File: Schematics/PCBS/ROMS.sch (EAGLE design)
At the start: 10 parts, among them IC1 ATMEGA328P-AU, M1 WIRELESS-NRF24L01-PA-EXT, Y1 16MHz

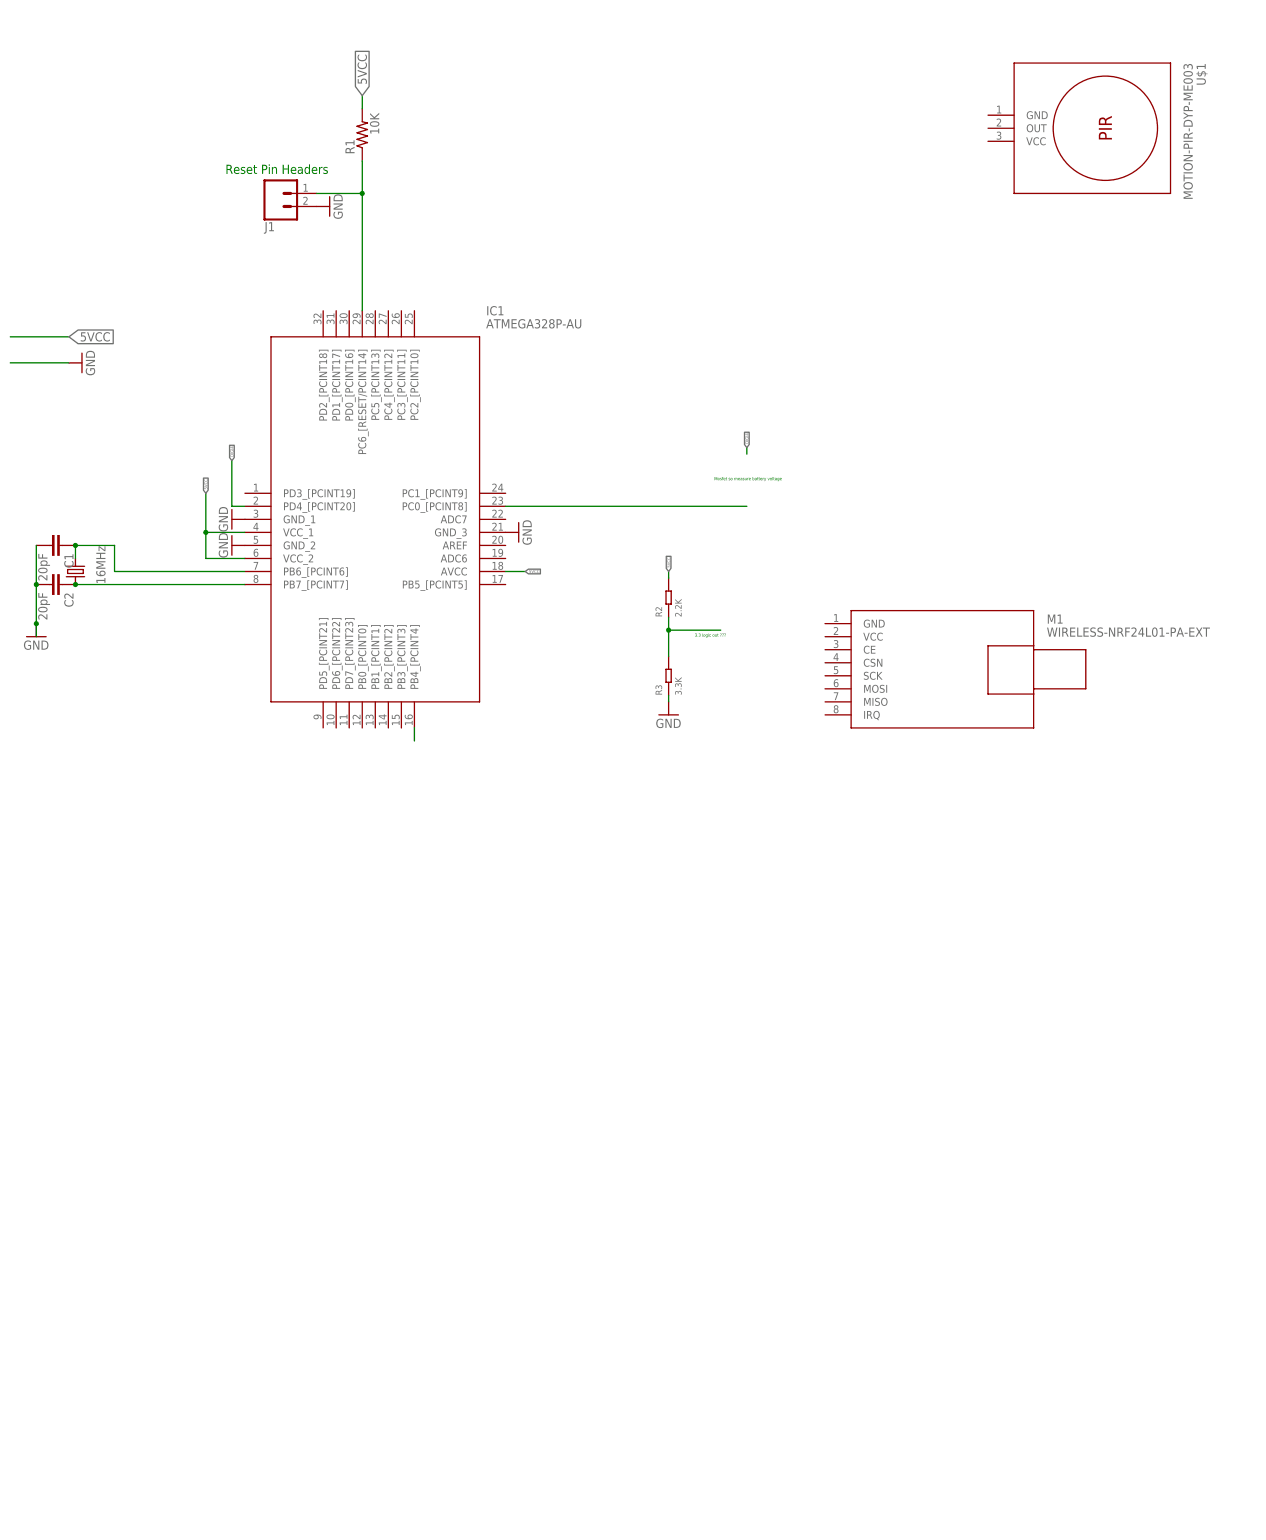
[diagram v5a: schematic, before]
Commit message: added header pins for IR Sensor
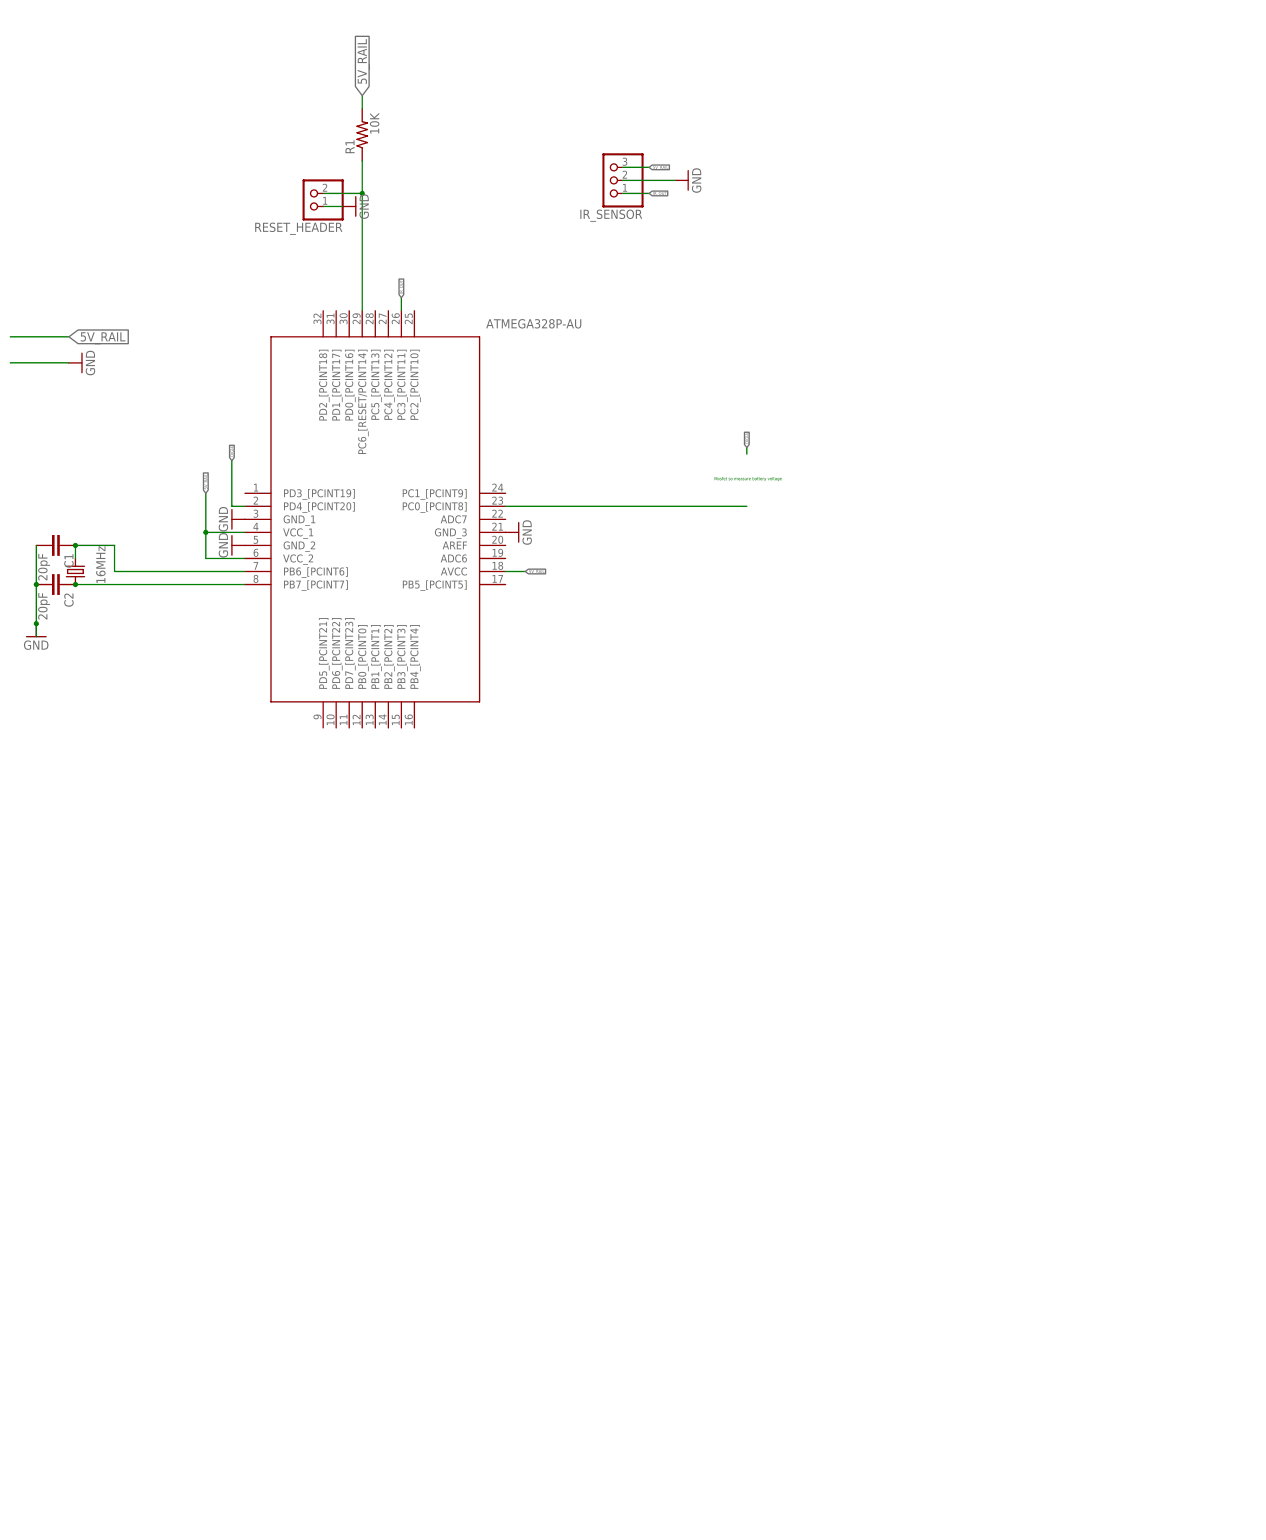
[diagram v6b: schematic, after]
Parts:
- removed J1: (no value), SparkFun-Connectors:CONN_02
- removed M1: WIRELESS-NRF24L01-PA-EXT, diy-modules:WIRELESS-NRF24L01-PA-EXT
- removed R2: 2.2K, Seeed-Resistor-2016:DIP-RES-2.2K-5%-1/4W(PR-D2.3XL6.5MM)
- removed R3: 3.3K, Seeed-Resistor-2016:DIP-RES-3.3K-5%-1/4W(PR-D2.3XL6.5MM)
- removed U$1: MOTION-PIR-DYP-ME003, diy-modules:MOTION-PIR-DYP-ME003
- added IR_SENSOR: (no value), adafruit:PINHD-1X3
- added RESET_HEADER: (no value), Connector:PINHD-1X2
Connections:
- removed net 5VCC: IC1.AVCC, IC1.VCC_1, IC1.VCC_2, R1.2, R2.2
- removed net N$5: R2.1, R3.2
- removed net N$6: IC1.PB4_[PCINT4]
- new net 5V_RAIL: IC1.AVCC, IC1.VCC_1, IC1.VCC_2, IR_SENSOR.3, R1.2
- new net IR_OUT: IC1.PC3_[PCINT11], IR_SENSOR.1
- net GND: now also IR_SENSOR.2, RESET_HEADER.1; no longer J1.2, R3.1
- net N$3: now also RESET_HEADER.2; no longer J1.1
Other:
- note removed: "3.3 logic out ???"
- note removed: "Reset Pin Headers"
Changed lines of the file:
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@@
 <?xml version="1.0" encoding="utf-8"?>
 <!DOCTYPE eagle SYSTEM "eagle.dtd">
-<eagle version="9.5.2">
+<eagle version="9.6.2">
 <drawing>
 <settings>
@@
 <part name="GND5" library="supply1" library_urn="urn:adsk.eagle:library:371" deviceset="GND" device=""/>
 <part name="R1" library="adafruit" library_urn="urn:adsk.eagle:library:420" deviceset="R-US_" device="0207/10" package3d_urn="urn:adsk.eagle:package:6240597/1" value="10K"/>
-<part name="J1" library="SparkFun-Connectors" deviceset="CONN_02" device=""/>
 <part name="GND6" library="supply1" library_urn="urn:adsk.eagle:library:371" deviceset="GND" device=""/>
-<part name="U$1" library="diy-modules" deviceset="MOTION-PIR-DYP-ME003" device=""/>
-<part name="M1" library="diy-modules" deviceset="WIRELESS-NRF24L01-PA-EXT" device=""/>
-<part name="R2" library="Seeed-Resistor-2016" deviceset="DIP-RES-2.2K-5%-1/4W(PR-D2.3XL6.5MM)" device="" value="2.2K"/>
-<part name="R3" library="Seeed-Resistor-2016" deviceset="DIP-RES-3.3K-5%-1/4W(PR-D2.3XL6.5MM)" device="" value="3.3K"/>
+<part name="IR_SENSOR" library="adafruit" library_urn="urn:adsk.eagle:library:420" deviceset="PINHD-1X3" device="" package3d_urn="urn:adsk.eagle:package:6240710/1"/>
 <part name="GND7" library="supply1" library_urn="urn:adsk.eagle:library:371" deviceset="GND" device=""/>
+<part name="RESET_HEADER" library="Connector" library_urn="urn:adsk.eagle:library:16378166" deviceset="PINHD-1X2" device="" package3d_urn="urn:adsk.eagle:package:22435/2"/>
 </parts>
 <sheets>
 <sheet>
 <plain>
-<text x="46.99" y="110.49" size="1.778" layer="91">Reset Pin Headers</text>
 <text x="142.24" y="50.8" size="0.6096" layer="91">Mosfet so measure battery voltage</text>
-<text x="138.43" y="20.32" size="0.6096" layer="91">3.3 logic out ???</text>
 </plain>
 <instances>
 <instance part="IC1" gate="G$1" x="50.8" y="48.26" smashed="yes">
-<attribute name="NAME" x="97.79" y="83.82" size="1.778" layer="95" align="center-left"/>
 <attribute name="VALUE" x="97.79" y="81.28" size="1.778" layer="96" align="center-left"/>
 </instance>
@@
 <attribute name="VALUE" x="76.962" y="118.11" size="1.778" layer="96" rot="R90"/>
 </instance>
-<instance part="J1" gate="G$1" x="57.15" y="106.68" smashed="yes" rot="MR180">
-<attribute name="VALUE" x="54.61" y="111.506" size="1.778" layer="96" font="vector" rot="MR180"/>
-<attribute name="NAME" x="54.61" y="101.092" size="1.778" layer="95" font="vector" rot="MR180"/>
-</instance>
-<instance part="GND6" gate="1" x="67.31" y="104.14" smashed="yes" rot="R90">
-<attribute name="VALUE" x="69.85" y="101.6" size="1.778" layer="96" rot="R90"/>
-</instance>
-<instance part="U$1" gate="G$1" x="215.9" y="119.38" smashed="yes" rot="R270">
-<attribute name="NAME" x="236.22" y="132.08" size="1.778" layer="95" rot="R270"/>
-<attribute name="VALUE" x="233.68" y="132.08" size="1.778" layer="96" rot="R270"/>
-</instance>
-<instance part="M1" gate="G$1" x="186.69" y="12.7" smashed="yes">
-<attribute name="NAME" x="207.01" y="22.86" size="1.778" layer="95"/>
-<attribute name="VALUE" x="207.01" y="20.32" size="1.778" layer="96"/>
-</instance>
-<instance part="R2" gate="G$1" x="133.35" y="27.94" smashed="yes" rot="R90">
-<attribute name="NAME" x="132.08" y="24.13" size="1.27" layer="95" ratio="10" rot="R90"/>
-<attribute name="VALUE" x="135.89" y="24.13" size="1.27" layer="96" ratio="10" rot="R90"/>
-</instance>
-<instance part="R3" gate="G$1" x="133.35" y="12.7" smashed="yes" rot="R90">
-<attribute name="NAME" x="132.08" y="8.89" size="1.27" layer="95" ratio="10" rot="R90"/>
-<attribute name="VALUE" x="135.89" y="8.89" size="1.27" layer="96" ratio="10" rot="R90"/>
-</instance>
-<instance part="GND7" gate="1" x="133.35" y="5.08" smashed="yes">
-<attribute name="VALUE" x="130.81" y="2.54" size="1.778" layer="96"/>
+<instance part="GND6" gate="1" x="72.39" y="104.14" smashed="yes" rot="R90">
+<attribute name="VALUE" x="74.93" y="101.6" size="1.778" layer="96" rot="R90"/>
+</instance>
+<instance part="IR_SENSOR" gate="A" x="121.92" y="109.22" smashed="yes" rot="R180">
+<attribute name="NAME" x="128.27" y="103.505" size="1.778" layer="95" rot="R180"/>
+<attribute name="VALUE" x="128.27" y="116.84" size="1.778" layer="96" rot="R180"/>
+</instance>
+<instance part="GND7" gate="1" x="137.16" y="109.22" smashed="yes" rot="R90">
+<attribute name="VALUE" x="139.7" y="106.68" size="1.778" layer="96" rot="R90"/>
+</instance>
+<instance part="RESET_HEADER" gate="G$1" x="63.5" y="106.68" smashed="yes" rot="R180">
+<attribute name="NAME" x="69.85" y="100.965" size="1.778" layer="95" rot="R180"/>
+<attribute name="VALUE" x="69.85" y="111.76" size="1.778" layer="96" rot="R180"/>
 </instance>
 </instances>
@@
 </segment>
 <segment>
-<pinref part="J1" gate="G$1" pin="2"/>
+<pinref part="IR_SENSOR" gate="A" pin="2"/>
+<wire x1="124.46" y1="109.22" x2="134.62" y2="109.22" width="0.1524" layer="91"/>
+<pinref part="GND7" gate="1" pin="GND"/>
+</segment>
+<segment>
 <pinref part="GND6" gate="1" pin="GND"/>
-</segment>
-<segment>
-<pinref part="R3" gate="G$1" pin="1"/>
-<pinref part="GND7" gate="1" pin="GND"/>
-<wire x1="133.35" y1="8.89" x2="133.35" y2="7.62" width="0.1524" layer="91"/>
-</segment>
-</net>
-<net name="5VCC" class="0">
+<pinref part="RESET_HEADER" gate="G$1" pin="1"/>
+<wire x1="69.85" y1="104.14" x2="66.04" y2="104.14" width="0.1524" layer="91"/>
+</segment>
+</net>
+<net name="N$3" class="0">
+<segment>
+<pinref part="IC1" gate="G$1" pin="PC6_[RESET/PCINT14]"/>
+<pinref part="R1" gate="G$1" pin="1"/>
+<wire x1="73.66" y1="83.82" x2="73.66" y2="106.68" width="0.1524" layer="91"/>
+<pinref part="RESET_HEADER" gate="G$1" pin="2"/>
+<wire x1="73.66" y1="106.68" x2="73.66" y2="113.03" width="0.1524" layer="91"/>
+<wire x1="73.66" y1="106.68" x2="66.04" y2="106.68" width="0.1524" layer="91"/>
+<junction x="73.66" y="106.68"/>
+</segment>
+</net>
+<net name="N$4" class="0">
+<segment>
+<pinref part="IC1" gate="G$1" pin="PC0_[PCINT8]"/>
+<wire x1="101.6" y1="45.72" x2="148.59" y2="45.72" width="0.1524" layer="91"/>
+</segment>
+</net>
+<net name="DIGI4" class="0">
+<segment>
+<pinref part="IC1" gate="G$1" pin="PD4_[PCINT20]"/>
+<wire x1="50.8" y1="45.72" x2="48.26" y2="45.72" width="0.1524" layer="91"/>
+<wire x1="48.26" y1="45.72" x2="48.26" y2="54.61" width="0.1524" layer="91"/>
+<label x="48.26" y="54.61" size="0.6096" layer="95" rot="R90" xref="yes"/>
+</segment>
+<segment>
+<wire x1="148.59" y1="55.88" x2="148.59" y2="57.15" width="0.1524" layer="91"/>
+<label x="148.59" y="57.15" size="0.6096" layer="95" rot="R90" xref="yes"/>
+</segment>
+</net>
+<net name="5V_RAIL" class="0">
 <segment>
 <wire x1="5.08" y1="78.74" x2="16.51" y2="78.74" width="0.1524" layer="91"/>
@@
 </segment>
 <segment>
-<pinref part="R2" gate="G$1" pin="2"/>
-<wire x1="133.35" y1="31.75" x2="133.35" y2="33.02" width="0.1524" layer="91"/>
-<label x="133.35" y="33.02" size="0.6096" layer="95" rot="R90" xref="yes"/>
-</segment>
-</net>
-<net name="N$3" class="0">
-<segment>
-<pinref part="IC1" gate="G$1" pin="PC6_[RESET/PCINT14]"/>
-<pinref part="R1" gate="G$1" pin="1"/>
-<wire x1="73.66" y1="83.82" x2="73.66" y2="106.68" width="0.1524" layer="91"/>
-<pinref part="J1" gate="G$1" pin="1"/>
-<wire x1="73.66" y1="106.68" x2="73.66" y2="113.03" width="0.1524" layer="91"/>
-<wire x1="64.77" y1="106.68" x2="73.66" y2="106.68" width="0.1524" layer="91"/>
-<junction x="73.66" y="106.68"/>
-</segment>
-</net>
-<net name="N$4" class="0">
-<segment>
-<pinref part="IC1" gate="G$1" pin="PC0_[PCINT8]"/>
-<wire x1="101.6" y1="45.72" x2="148.59" y2="45.72" width="0.1524" layer="91"/>
-</segment>
-</net>
-<net name="DIGI4" class="0">
-<segment>
-<pinref part="IC1" gate="G$1" pin="PD4_[PCINT20]"/>
-<wire x1="50.8" y1="45.72" x2="48.26" y2="45.72" width="0.1524" layer="91"/>
-<wire x1="48.26" y1="45.72" x2="48.26" y2="54.61" width="0.1524" layer="91"/>
-<label x="48.26" y="54.61" size="0.6096" layer="95" rot="R90" xref="yes"/>
-</segment>
-<segment>
-<wire x1="148.59" y1="55.88" x2="148.59" y2="57.15" width="0.1524" layer="91"/>
-<label x="148.59" y="57.15" size="0.6096" layer="95" rot="R90" xref="yes"/>
-</segment>
-</net>
-<net name="N$5" class="0">
-<segment>
-<pinref part="R3" gate="G$1" pin="2"/>
-<pinref part="R2" gate="G$1" pin="1"/>
-<wire x1="133.35" y1="16.51" x2="133.35" y2="21.59" width="0.1524" layer="91"/>
-<wire x1="133.35" y1="21.59" x2="133.35" y2="24.13" width="0.1524" layer="91"/>
-<wire x1="133.35" y1="21.59" x2="143.51" y2="21.59" width="0.1524" layer="91"/>
-<junction x="133.35" y="21.59"/>
-</segment>
-</net>
-<net name="N$6" class="0">
-<segment>
-<pinref part="IC1" gate="G$1" pin="PB4_[PCINT4]"/>
-<wire x1="83.82" y1="2.54" x2="83.82" y2="0" width="0.1524" layer="91"/>
-</segment>
-</net>
+<pinref part="IR_SENSOR" gate="A" pin="3"/>
+<wire x1="124.46" y1="111.76" x2="129.54" y2="111.76" width="0.1524" layer="91"/>
+<label x="129.54" y="111.76" size="0.6096" layer="95" xref="yes"/>
+</segment>
+</net>
+<net name="IR_OUT" class="0">
+<segment>
+<pinref part="IR_SENSOR" gate="A" pin="1"/>
+<wire x1="124.46" y1="106.68" x2="129.54" y2="106.68" width="0.1524" layer="91"/>
+<label x="129.54" y="106.68" size="0.6096" layer="95" xref="yes"/>
+</segment>
+<segment>
+<pinref part="IC1" gate="G$1" pin="PC3_[PCINT11]"/>
+<wire x1="81.28" y1="83.82" x2="81.28" y2="86.36" width="0.1524" layer="91"/>
+<label x="81.28" y="86.36" size="0.6096" layer="95" rot="R90" xref="yes"/>
+</segment>
+</net>
